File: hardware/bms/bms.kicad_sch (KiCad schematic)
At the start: 34 parts, among them J1 Screw_Terminal_01x01, J10 Conn_01x10, J11 USB_C_Receptacle_USB2.0, J12 Conn_01x03, J13 Conn_01x07, J2 Screw_Terminal_01x01, J3 Screw_Terminal_01x01, J4 Screw_Terminal_01x01, J5 Screw_Terminal_01x01, J6 Conn_01x02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

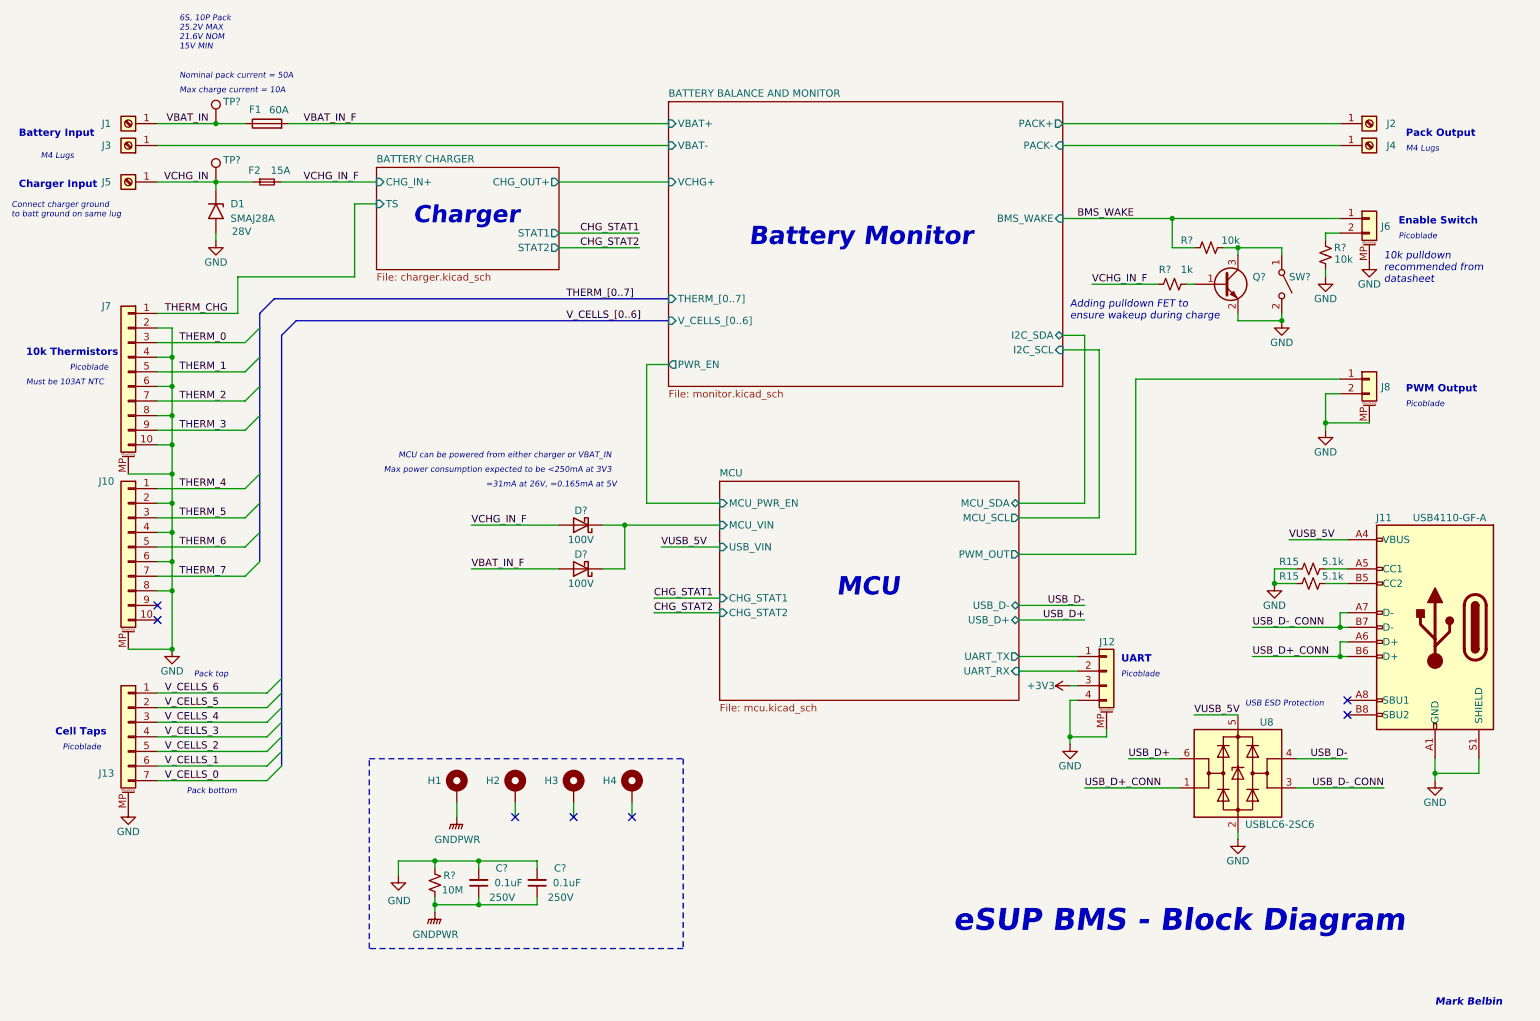
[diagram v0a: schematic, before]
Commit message: Added Micro SD card circuit.
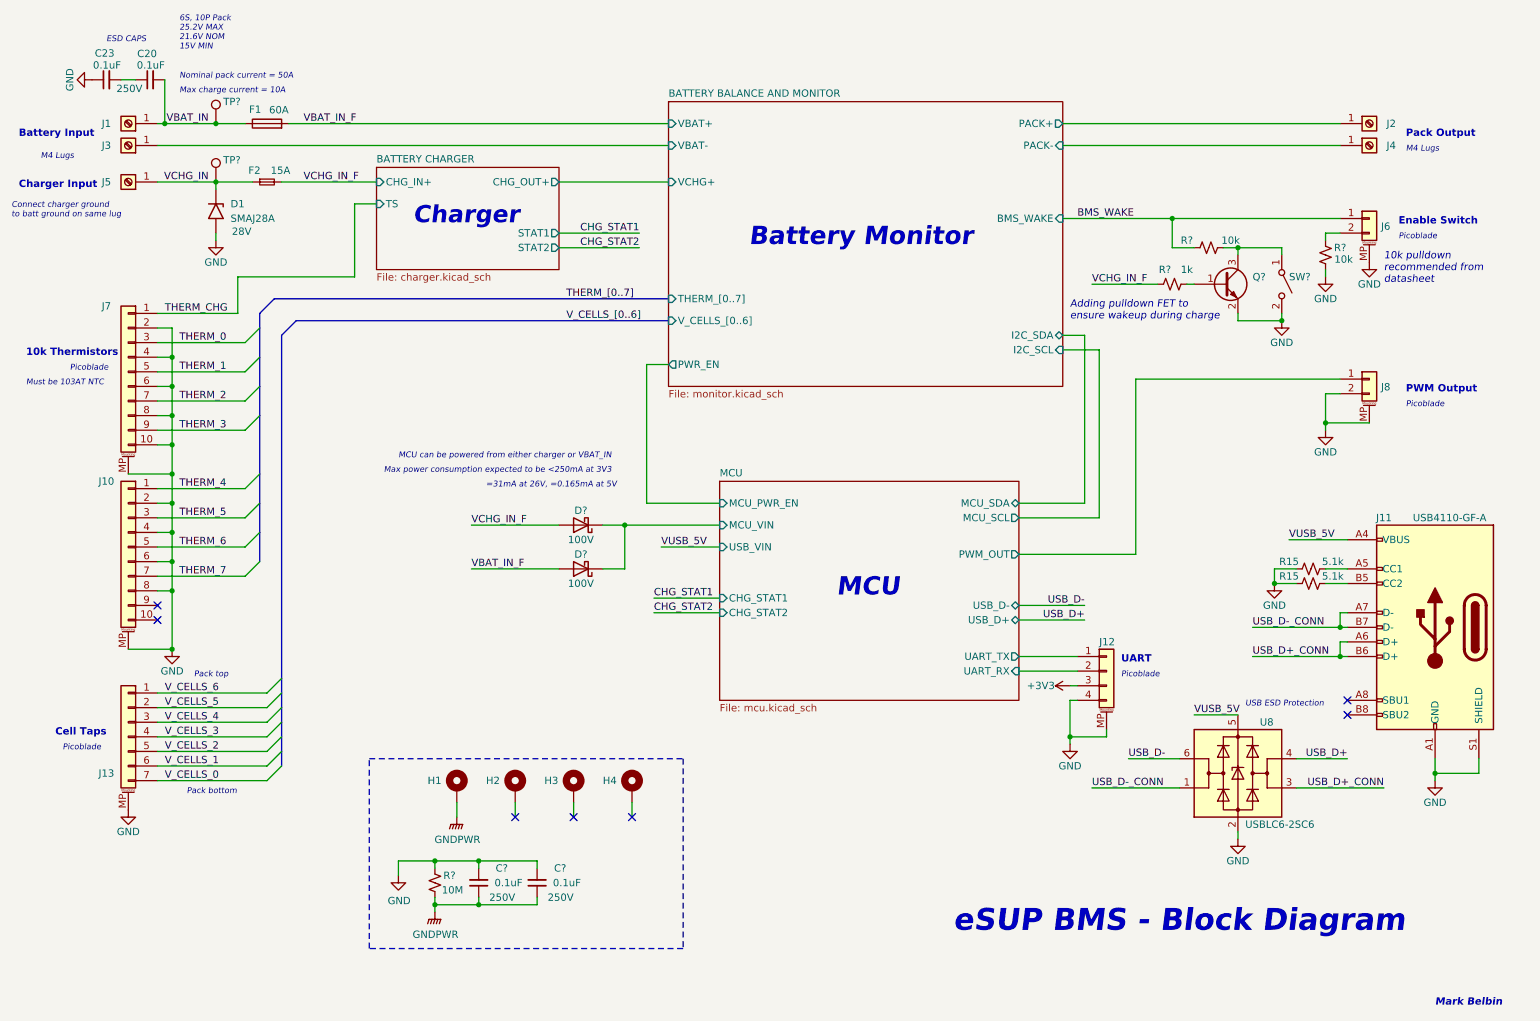
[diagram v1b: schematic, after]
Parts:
- added C20, C23: 0.1uF, Capacitor_SMD:C_0805_2012Metric, symbol Device:C_Small
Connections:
- net GND: now also C23.1
- net USB_D+: now also U8.4 (I/O2); no longer U8.6 (I/O1)
- net USB_D+_CONN: now also U8.3 (I/O2); no longer U8.1 (I/O1)
- net USB_D-: now also U8.6 (I/O1); no longer U8.4 (I/O2)
- net USB_D-_CONN: now also U8.1 (I/O1); no longer U8.3 (I/O2)
- net VBAT_IN: now also C20.2
- new net: C20.1, C23.2
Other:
- note added: "ESD CAPS"
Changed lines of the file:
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@@
   (junction (at 54.61 46.99) (diameter 0) (color 0 0 0 0)
+  )
+  (junction (at 45.72 36.83) (diameter 0) (color 0 0 0 0)
   )
   (junction (at 46.99 107.95) (diameter 0) (color 0 0 0 0)
@@
     (stroke (width 0) (type default))
   )
+  (wire (pts (xy 45.72 36.83) (xy 54.61 36.83))
+    (stroke (width 0) (type default))
+  )
   (bus (pts (xy 66.04 135.89) (xy 66.04 138.43))
     (stroke (width 0) (type default))
@@
     (stroke (width 0) (type default))
   )
-  (wire (pts (xy 242.57 147.32) (xy 251.46 147.32))
+  (wire (pts (xy 222.25 147.32) (xy 213.36 147.32))
     (stroke (width 0) (type default))
   )
@@
     (stroke (width 0) (type default))
   )
+  (wire (pts (xy 45.72 29.21) (xy 45.72 36.83))
+    (stroke (width 0) (type default))
+  )
   (bus (pts (xy 62.23 69.85) (xy 62.23 72.39))
     (stroke (width 0) (type default))
@@
     (stroke (width 0) (type default))
   )
+  (wire (pts (xy 40.64 29.21) (xy 38.1 29.21))
+    (stroke (width 0) (type default))
+  )
   (wire (pts (xy 208.28 105.41) (xy 194.31 105.41))
     (stroke (width 0) (type default))
@@
     (stroke (width 0) (type default))
   )
-  (wire (pts (xy 213.36 147.32) (xy 222.25 147.32))
+  (wire (pts (xy 242.57 147.32) (xy 251.46 147.32))
     (stroke (width 0) (type default))
   )
@@
     (stroke (width 0) (type default))
   )
+  (wire (pts (xy 207.01 152.4) (xy 222.25 152.4))
+    (stroke (width 0) (type default))
+  )
+  (bus (pts (xy 66.04 146.05) (xy 66.04 148.59))
+    (stroke (width 0) (type default))
+  )
   (wire (pts (xy 242.57 152.4) (xy 257.81 152.4))
-    (stroke (width 0) (type default))
-  )
-  (bus (pts (xy 66.04 146.05) (xy 66.04 148.59))
-    (stroke (width 0) (type default))
-  )
-  (wire (pts (xy 205.74 152.4) (xy 222.25 152.4))
     (stroke (width 0) (type default))
   )
@@
     (stroke (width 0) (type default))
   )
-  (wire (pts (xy 44.45 36.83) (xy 54.61 36.83))
+  (wire (pts (xy 44.45 36.83) (xy 45.72 36.83))
     (stroke (width 0) (type default))
   )
@@
     (effects (font (size 1.016 1.016) italic) (justify left bottom))
   )
+  (text "ESD CAPS" (at 35.56 22.86 0)
+    (effects (font (size 1.016 1.016) italic) (justify left bottom))
+  )
   (text "Battery Input" (at 20.32 39.37 0)
     (effects (font (size 1.27 1.27) (thickness 0.254) bold) (justify left bottom))
@@
     (effects (font (size 1.27 1.27)) (justify right bottom))
   )
-  (label "USB_D+_CONN" (at 205.74 152.4 0) (fields_autoplaced)
-    (effects (font (size 1.27 1.27)) (justify left bottom))
+  (label "USB_D+_CONN" (at 257.81 152.4 180) (fields_autoplaced)
+    (effects (font (size 1.27 1.27)) (justify right bottom))
   )
   (label "THERM_2" (at 48.26 85.09 0) (fields_autoplaced)
@@
     (effects (font (size 1.27 1.27)) (justify right bottom))
   )
-  (label "USB_D-_CONN" (at 257.81 152.4 180) (fields_autoplaced)
+  (label "USB_D-_CONN" (at 207.01 152.4 0) (fields_autoplaced)
+    (effects (font (size 1.27 1.27)) (justify left bottom))
+  )
+  (label "V_CELLS_[0..6]" (at 115.57 71.12 0) (fields_autoplaced)
+    (effects (font (size 1.27 1.27)) (justify left bottom))
+  )
+  (label "BMS_WAKE" (at 204.47 53.34 0) (fields_autoplaced)
+    (effects (font (size 1.27 1.27)) (justify left bottom))
+  )
+  (label "THERM_1" (at 48.26 80.01 0) (fields_autoplaced)
+    (effects (font (size 1.27 1.27)) (justify left bottom))
+  )
+  (label "V_CELLS_2" (at 45.72 146.05 0) (fields_autoplaced)
+    (effects (font (size 1.27 1.27)) (justify left bottom))
+  )
+  (label "USB_D+_CONN" (at 234.95 129.54 0) (fields_autoplaced)
+    (effects (font (size 1.27 1.27)) (justify left bottom))
+  )
+  (label "USB_D+" (at 251.46 147.32 180) (fields_autoplaced)
     (effects (font (size 1.27 1.27)) (justify right bottom))
-  )
-  (label "V_CELLS_[0..6]" (at 115.57 71.12 0) (fields_autoplaced)
-    (effects (font (size 1.27 1.27)) (justify left bottom))
-  )
-  (label "BMS_WAKE" (at 204.47 53.34 0) (fields_autoplaced)
-    (effects (font (size 1.27 1.27)) (justify left bottom))
-  )
-  (label "THERM_1" (at 48.26 80.01 0) (fields_autoplaced)
-    (effects (font (size 1.27 1.27)) (justify left bottom))
-  )
-  (label "V_CELLS_2" (at 45.72 146.05 0) (fields_autoplaced)
-    (effects (font (size 1.27 1.27)) (justify left bottom))
-  )
-  (label "USB_D+_CONN" (at 234.95 129.54 0) (fields_autoplaced)
-    (effects (font (size 1.27 1.27)) (justify left bottom))
-  )
-  (label "USB_D+" (at 213.36 147.32 0) (fields_autoplaced)
-    (effects (font (size 1.27 1.27)) (justify left bottom))
   )
   (label "VCHG_IN_F" (at 69.85 46.99 0) (fields_autoplaced)
@@
     (effects (font (size 1.27 1.27)) (justify left bottom))
   )
-  (label "USB_D-" (at 251.46 147.32 180) (fields_autoplaced)
-    (effects (font (size 1.27 1.27)) (justify right bottom))
+  (label "USB_D-" (at 213.36 147.32 0) (fields_autoplaced)
+    (effects (font (size 1.27 1.27)) (justify left bottom))
   )
   (label "USB_D+" (at 205.74 123.19 180) (fields_autoplaced)
@@
     )
   )
+  (symbol (lib_id "Device:C_Small") (at 43.18 29.21 90) (unit 1)
+    (in_bom yes) (on_board yes) (dnp no)
+    (property "Reference" "C20" (at 44.3515 24.6695 90)
+      (effects (font (size 1.27 1.27)) (justify left))
+    )
+    (property "Value" "0.1uF" (at 45.72 26.67 90)
+      (effects (font (size 1.27 1.27)) (justify left))
+    )
+    (property "Footprint" "Capacitor_SMD:C_0805_2012Metric" (at 43.18 29.21 0)
+      (effects (font (size 1.27 1.27)) hide)
+    )
+    (property "Datasheet" "~" (at 43.18 29.21 0)
+      (effects (font (size 1.27 1.27)) hide)
+    )
+    (property "MFG" "TDK Corporation" (at 43.18 29.21 0)
+      (effects (font (size 1.27 1.27)) hide)
+    )
+    (property "MFG PN" "CGA4J3X7T2E104K125AA" (at 43.18 29.21 0)
+      (effects (font (size 1.27 1.27)) hide)
+    )
+    (property "Voltage" "250V" (at 45.4914 26.8732 0)
+      (effects (font (size 1.27 1.27)) (justify left) hide)
+    )
+    (pin "1")
+    (pin "2")
+    (instances
+      (project "bms"
+        (path "/a4805e9d-b940-444e-a7cb-db4f4c53ed46/00000000-0000-0000-0000-00006523a805"
+          (reference "C20") (unit 1)
+        )
+        (path "/a4805e9d-b940-444e-a7cb-db4f4c53ed46"
+          (reference "C7") (unit 1)
+        )
+      )
+    )
+  )
   (symbol (lib_id "power:GND") (at 54.61 57.15 0) (unit 1)
     (in_bom yes) (on_board yes) (dnp no)
@@
         (path "/a4805e9d-b940-444e-a7cb-db4f4c53ed46"
           (reference "#PWR094") (unit 1)
+        )
+      )
+    )
+  )
+  (symbol (lib_id "power:GND") (at 33.02 29.21 270) (unit 1)
+    (in_bom yes) (on_board yes) (dnp no)
+    (property "Reference" "#PWR080" (at 26.67 29.21 0)
+      (effects (font (size 1.27 1.27)) hide)
+    )
+    (property "Value" "GND" (at 29.21 29.21 0)
+      (effects (font (size 1.27 1.27)))
+    )
+    (property "Footprint" "" (at 33.02 29.21 0)
+      (effects (font (size 1.27 1.27)) hide)
+    )
+    (property "Datasheet" "" (at 33.02 29.21 0)
+      (effects (font (size 1.27 1.27)) hide)
+    )
+    (pin "1")
+    (instances
+      (project "bms"
+        (path "/a4805e9d-b940-444e-a7cb-db4f4c53ed46/00000000-0000-0000-0000-00006523a805"
+          (reference "#PWR080") (unit 1)
+        )
+        (path "/a4805e9d-b940-444e-a7cb-db4f4c53ed46"
+          (reference "#PWR073") (unit 1)
         )
       )
@@
         )
       )
+    )
+  )
+  (symbol (lib_id "Device:C_Small") (at 35.56 29.21 90) (unit 1)
+    (in_bom yes) (on_board yes) (dnp no)
+    (property "Reference" "C23" (at 36.9681 24.5905 90)
+      (effects (font (size 1.27 1.27)) (justify left))
+    )
+    (property "Value" "0.1uF" (at 38.1 26.67 90)
+      (effects (font (size 1.27 1.27)) (justify left))
+    )
+    (property "Footprint" "Capacitor_SMD:C_0805_2012Metric" (at 35.56 29.21 0)
+      (effects (font (size 1.27 1.27)) hide)
+    )
+    (property "Datasheet" "~" (at 35.56 29.21 0)
+      (effects (font (size 1.27 1.27)) hide)
+    )
+    (property "MFG" "TDK Corporation" (at 35.56 29.21 0)
+      (effects (font (size 1.27 1.27)) hide)
+    )
+    (property "MFG PN" "CGA4J3X7T2E104K125AA" (at 35.56 29.21 0)
+      (effects (font (size 1.27 1.27)) hide)
+    )
+    (property "Voltage" "250V" (at 41.8246 30.7499 90)
+      (effects (font (size 1.27 1.27)) (justify left))
+    )
+    (pin "1")
+    (pin "2")
+    (instances
+      (project "bms"
+        (path "/a4805e9d-b940-444e-a7cb-db4f4c53ed46/00000000-0000-0000-0000-00006523a805"
+          (reference "C23") (unit 1)
+        )
+        (path "/a4805e9d-b940-444e-a7cb-db4f4c53ed46"
+          (reference "C6") (unit 1)
+        )
+      )

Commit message: Added extra features to try and prevent SD card data corruption. Added override enable so that the MCU can keep itself on until the SD card is finished writing, also added 5V / wake detect circuit so the MCU can begin to sense when the 5V rail is dropping and react accordingly
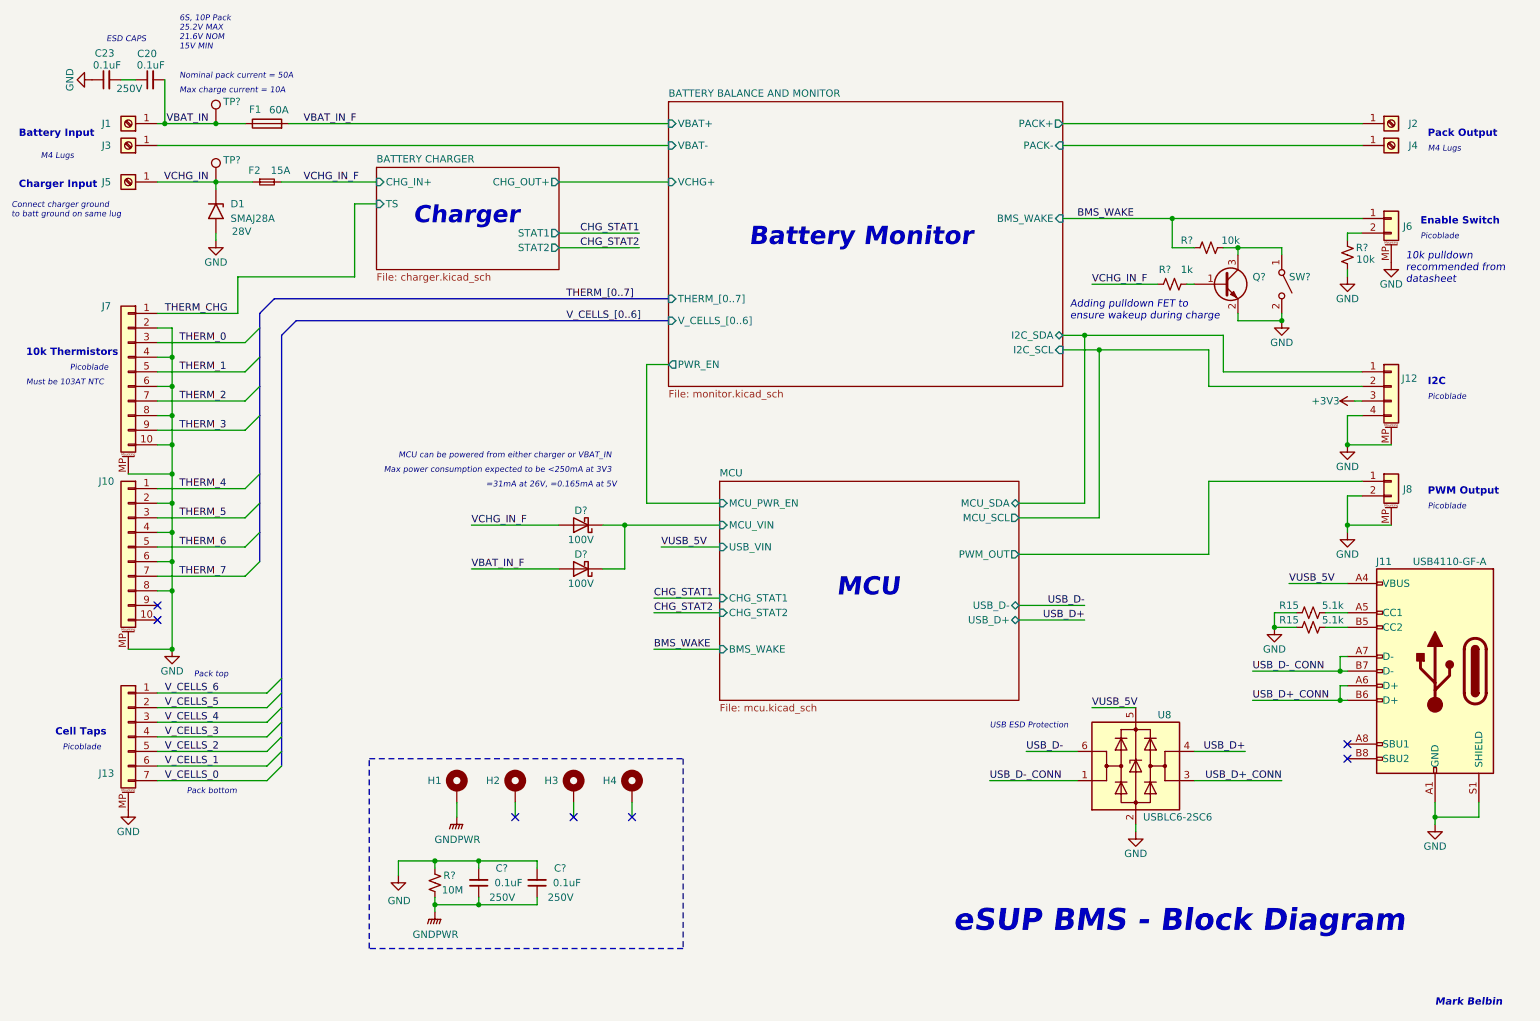
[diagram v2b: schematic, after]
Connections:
- net MCU/UART_RX is gone; now on net BATTERY BALANCE AND MONITOR/I2C_SCL: J12.2 (Pin_2)
- net MCU/UART_TX is gone; now on net BATTERY BALANCE AND MONITOR/I2C_SDA: J12.1 (Pin_1)
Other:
- sheet MCU ports: added BMS_WAKE; removed UART_RX, UART_TX
- note added: "I2C"
- note removed: "UART"
- moved on the sheet: J11, J2, J4, J6, J8, R15, R?, U8

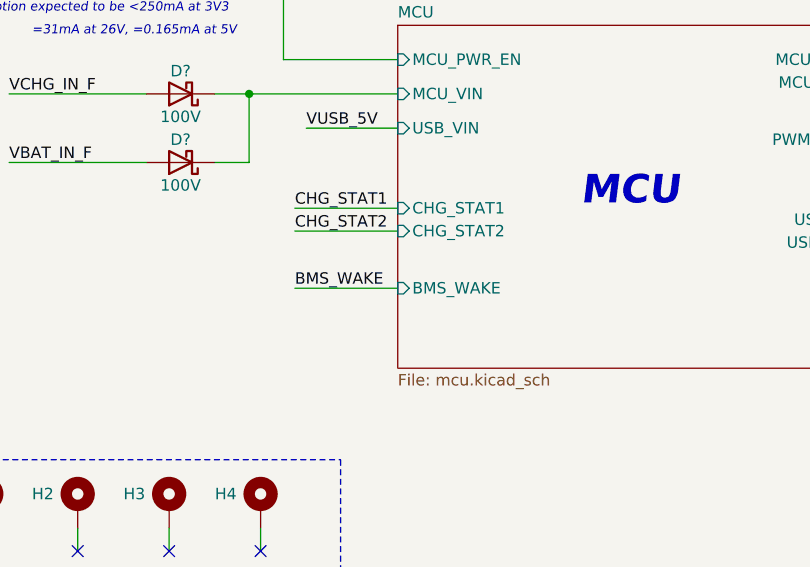
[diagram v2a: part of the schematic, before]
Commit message: Added bulk cap for 5V and 3V3 rails, made sure they fit in current layout
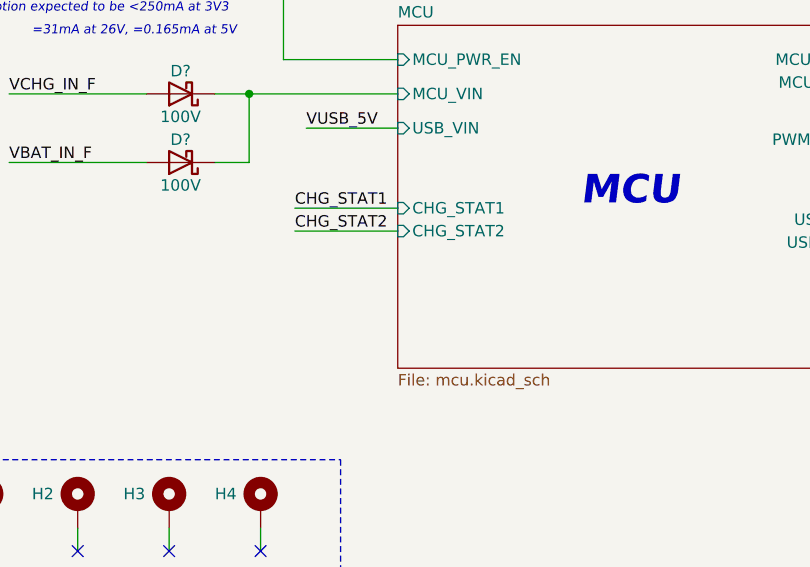
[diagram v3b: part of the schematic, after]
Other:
- sheet MCU ports: added none; removed BMS_WAKE
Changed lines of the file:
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@@
-    (stroke (width 0) (type default))
-  )
-  (wire (pts (xy 130.81 128.27) (xy 142.24 128.27))
     (stroke (width 0) (type default))
   )
@@
   )
   (label "CHG_STAT2" (at 130.81 121.92 0) (fields_autoplaced)
-    (effects (font (size 1.27 1.27)) (justify left bottom))
-  )
-  (label "BMS_WAKE" (at 130.81 128.27 0) (fields_autoplaced)
     (effects (font (size 1.27 1.27)) (justify left bottom))
   )
@@
       (effects (font (size 1.27 1.27)) (justify left))
     )
-    (pin "BMS_WAKE" input (at 142.24 128.27 180)
-      (effects (font (size 1.27 1.27)) (justify left))
-    )
